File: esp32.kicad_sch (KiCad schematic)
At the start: 20 parts, among them J2 TC2030-IDC, J3 Conn_01x04, J4 Conn_01x06, J5 USB_C_Receptacle_USB2.0, SW1 GT-TC029B-H025-L1N, SW2 GT-TC029B-H025-L1N, U3 RT9080-33GJ5, U4 ESP32-S3-WROOM-1

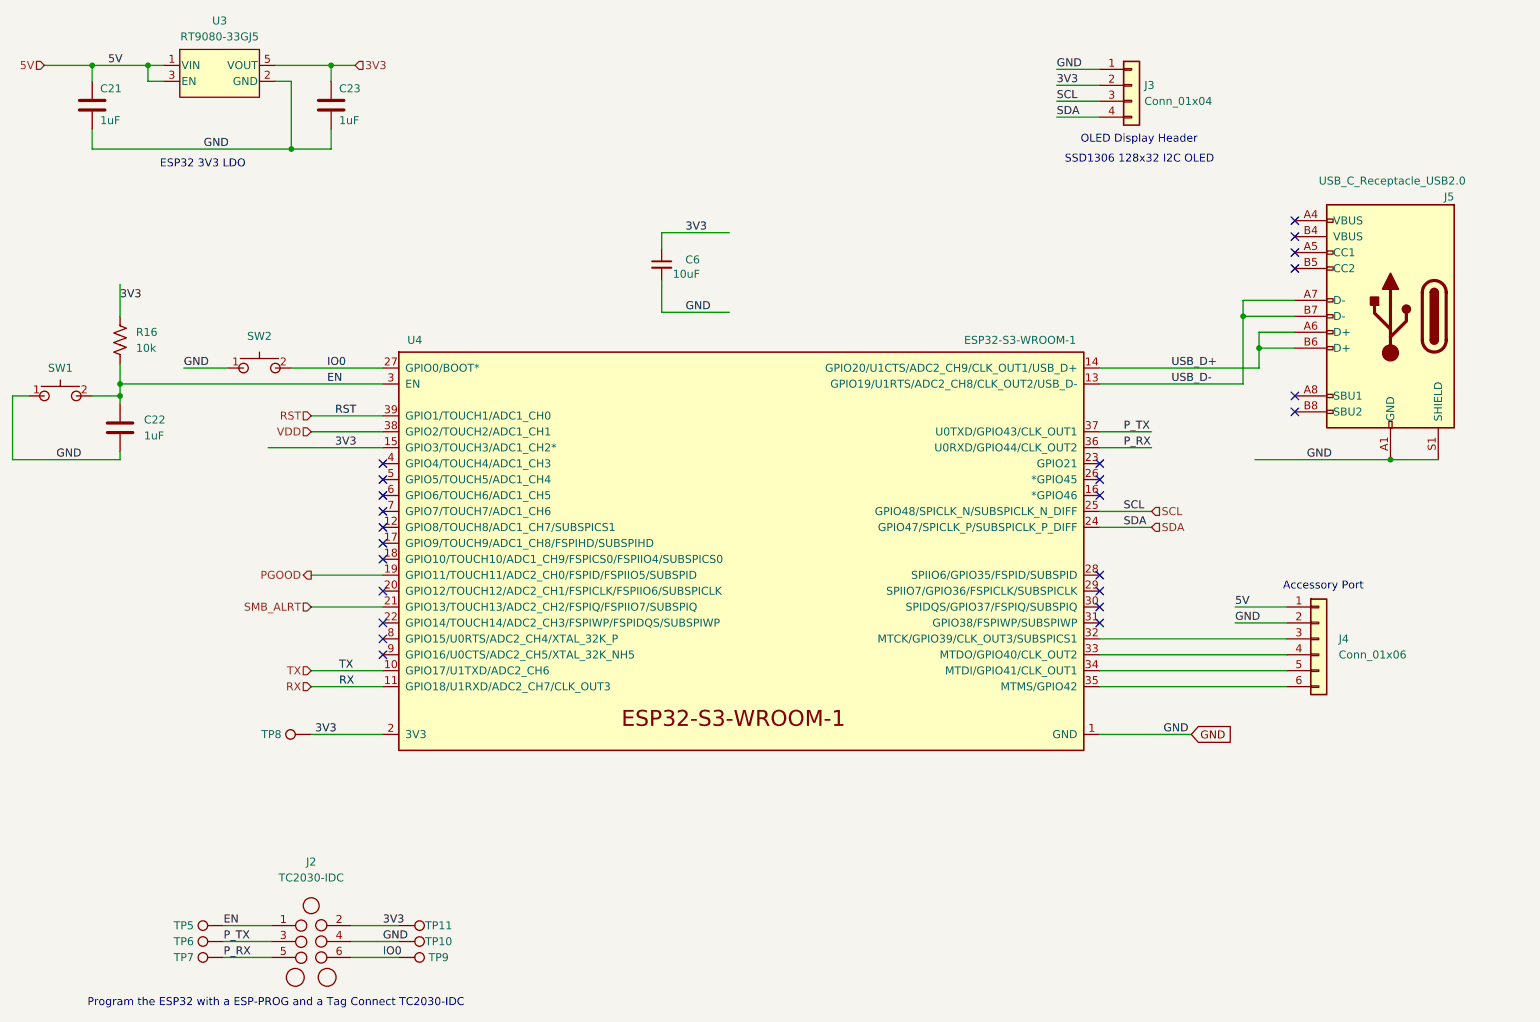
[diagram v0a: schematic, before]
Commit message: added pullup resistors for #25
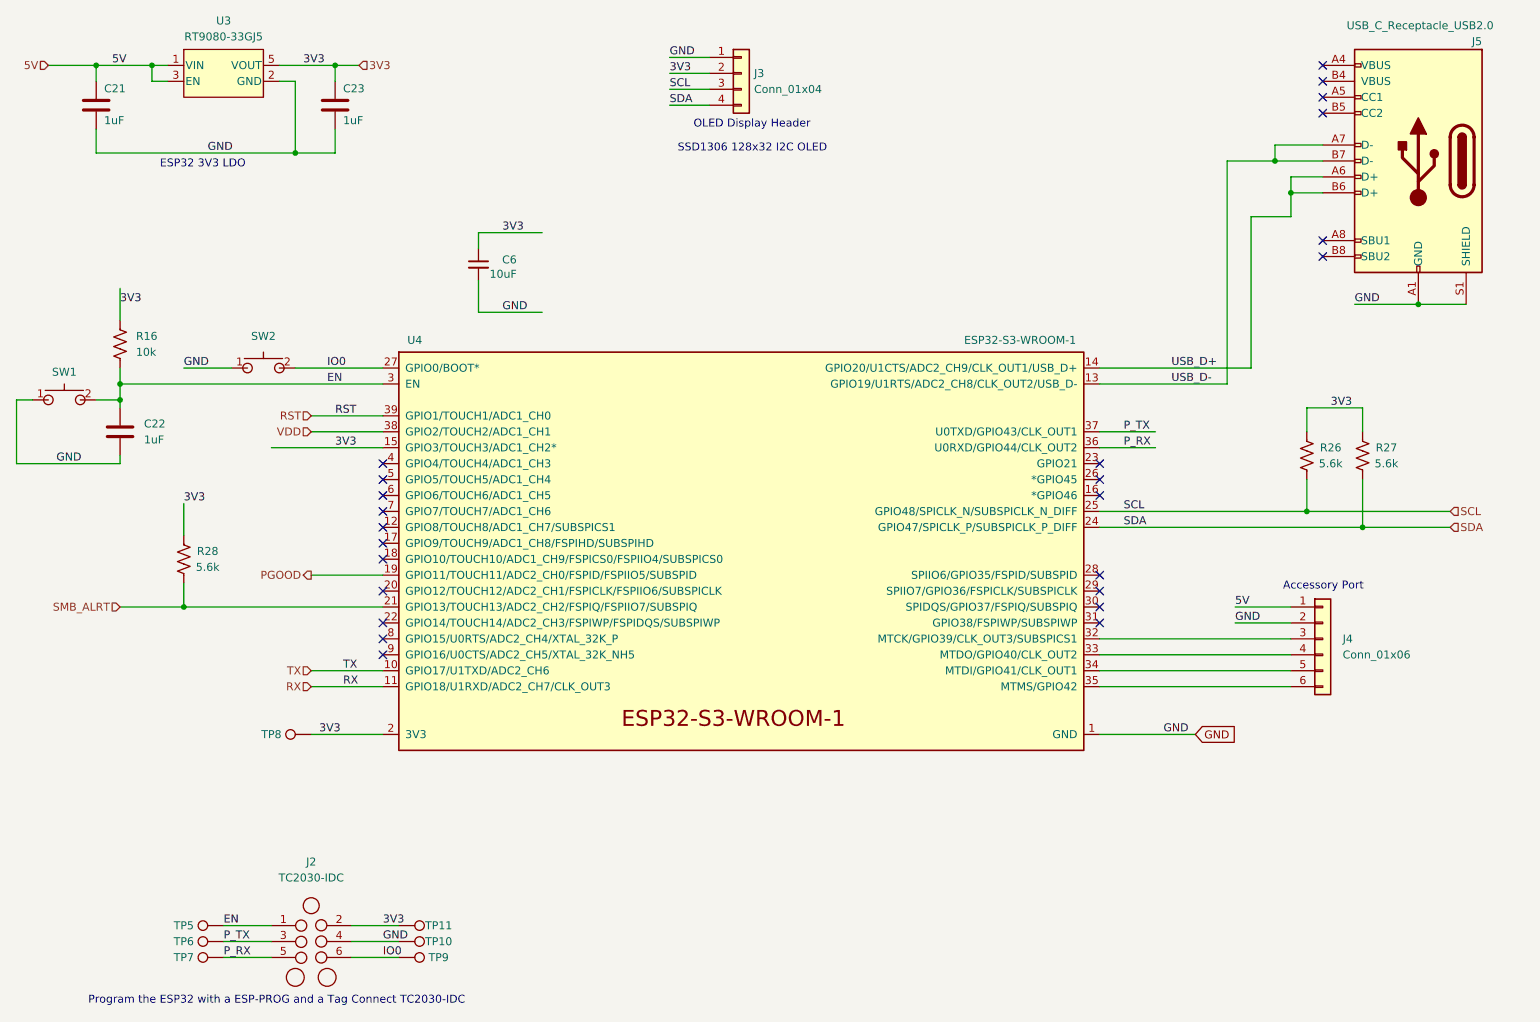
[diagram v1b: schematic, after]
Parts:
- added R26, R27, R28: 5.6k, Resistor_SMD:R_0402_1005Metric, symbol Device:R_US
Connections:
- net 3V3: now also R26.2, R27.2, R28.2
- net SCL: now also R26.1
- net SDA: now also R27.1
- net SMB_ALRT: now also R28.1
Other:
- moved on the sheet: C21, C22, C23, C6, J3, J4, J5, R16, SW1, SW2, U3

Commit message: Revert "added pullup resistors for #25"
This reverts commit 91572af801fdd590416a5d3df79444bb16faa4cf.
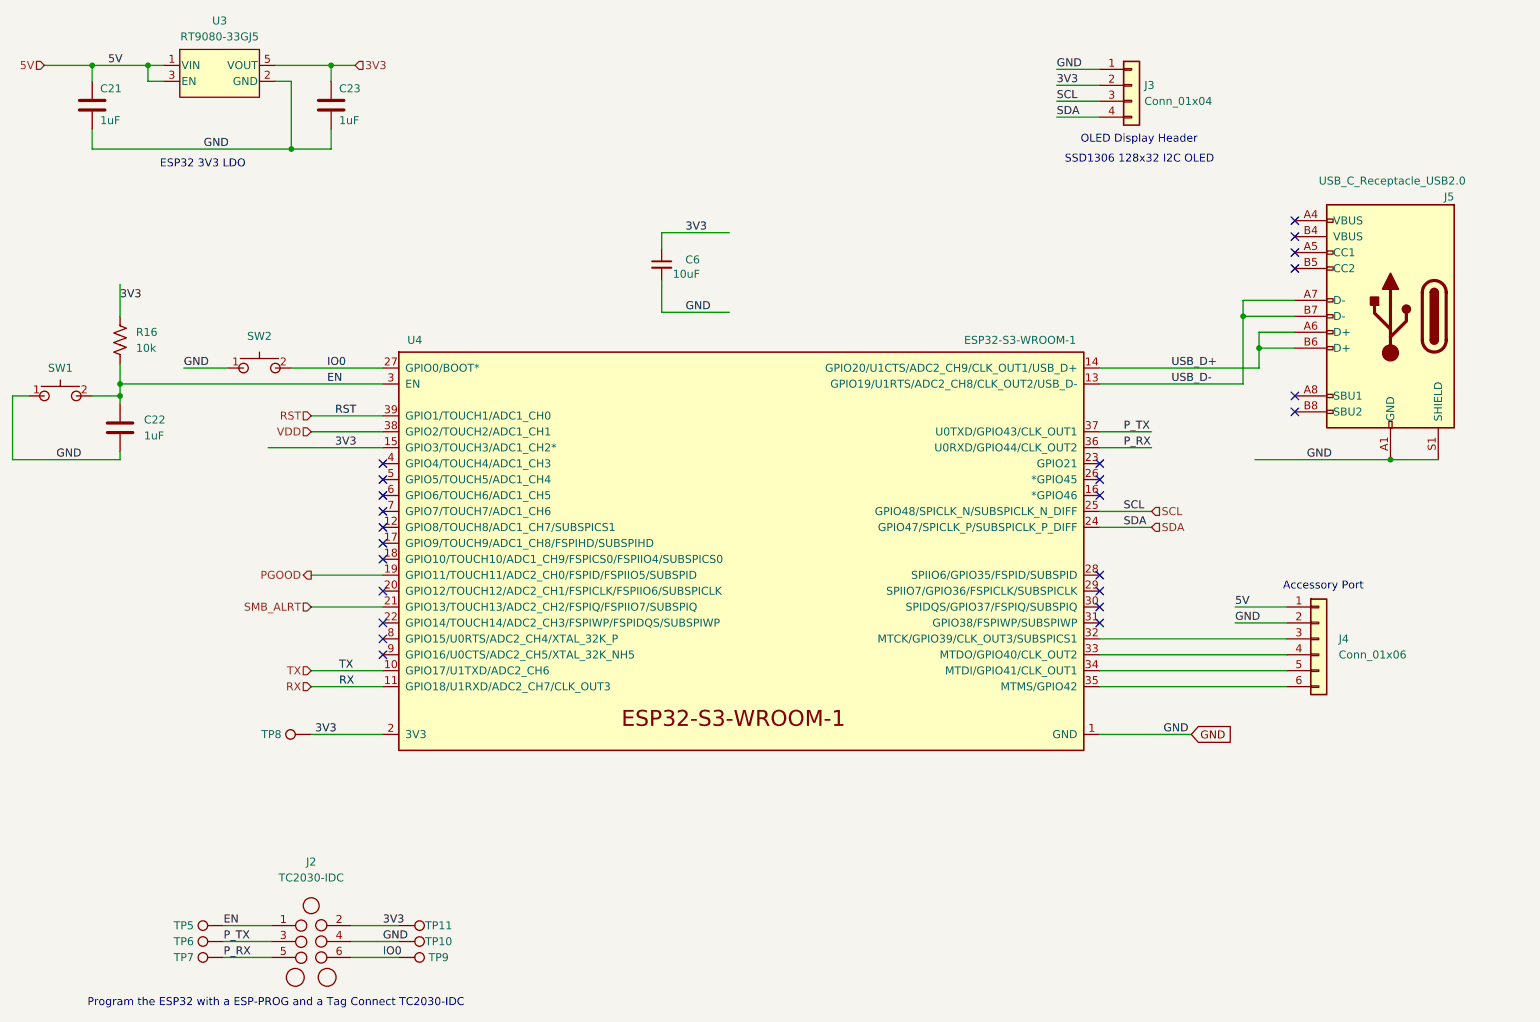
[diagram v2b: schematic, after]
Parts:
- removed R26, R27, R28: 5.6k, Resistor_SMD:R_0402_1005Metric, symbol Device:R_US
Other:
- moved on the sheet: C21, C22, C23, C6, J3, J4, J5, R16, SW1, SW2, U3
